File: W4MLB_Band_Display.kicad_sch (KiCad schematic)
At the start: 15 parts, among them J1 SSW-115-01-G-S, J2 SSW-115-01-G-S, J3 SSQ-108-01-T-D-LL, J4 SAMTEC-TST-108-01-X-D, J5 EJ503B, J6 796683-2, J7 PJRAN1X1U01X, J8 PJRAN1X1U01X, J9 Conn_01x10_Pin, U1 ESP32-DEVKIT-V1

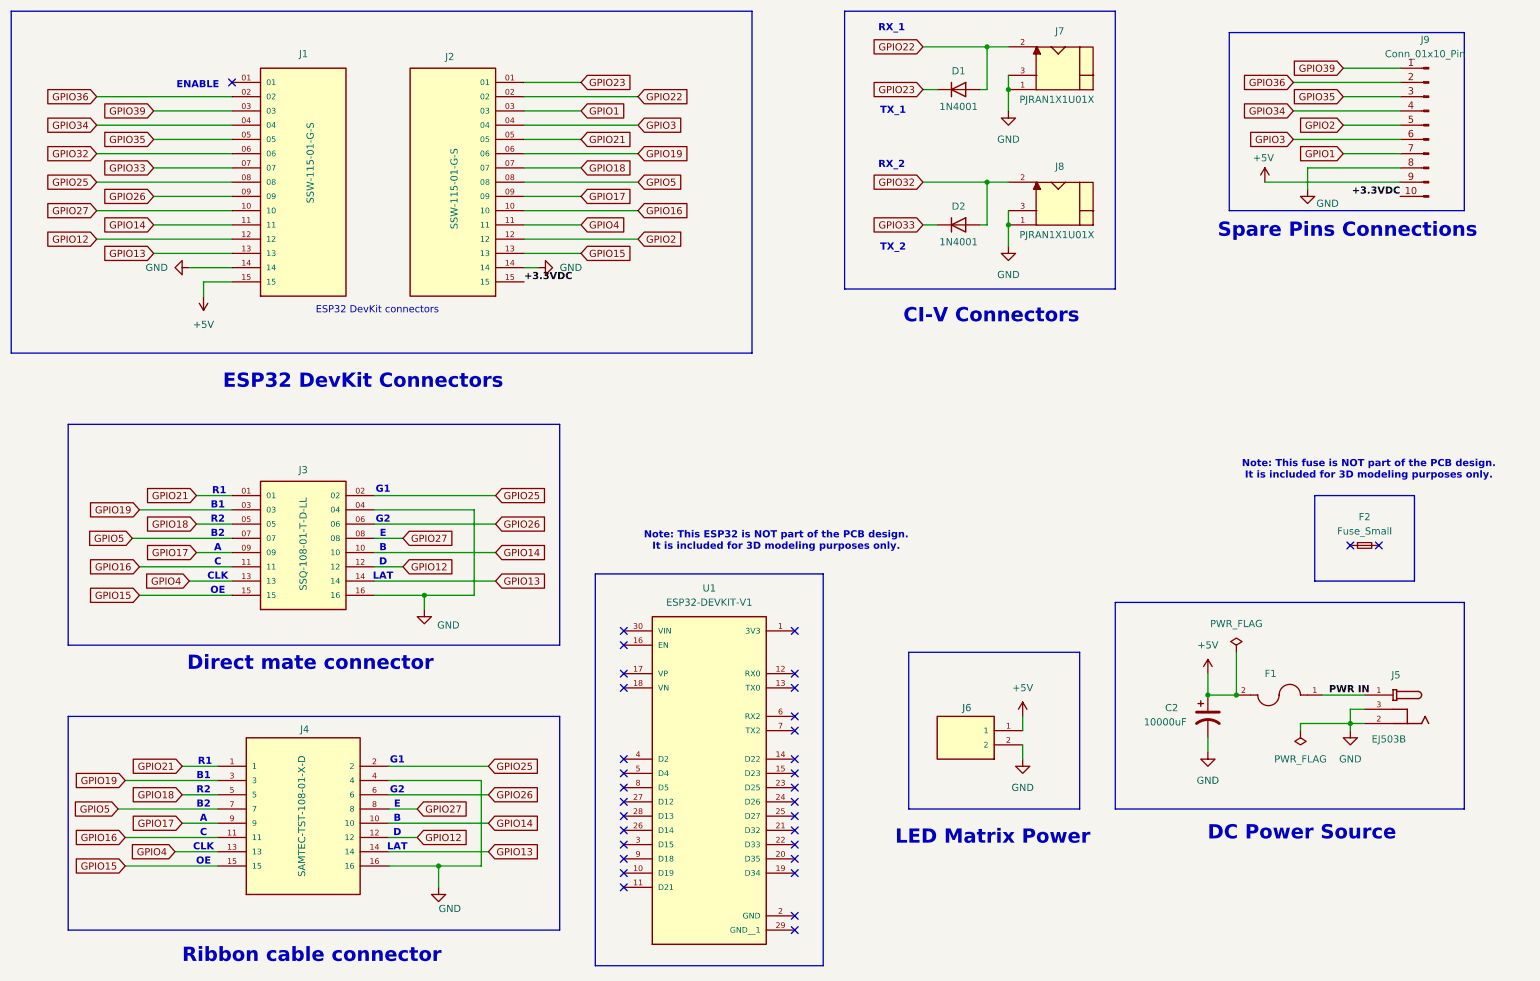
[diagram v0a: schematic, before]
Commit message: First release candidate draft
Laid out components and routed signals. Added silkscreen text and artwork
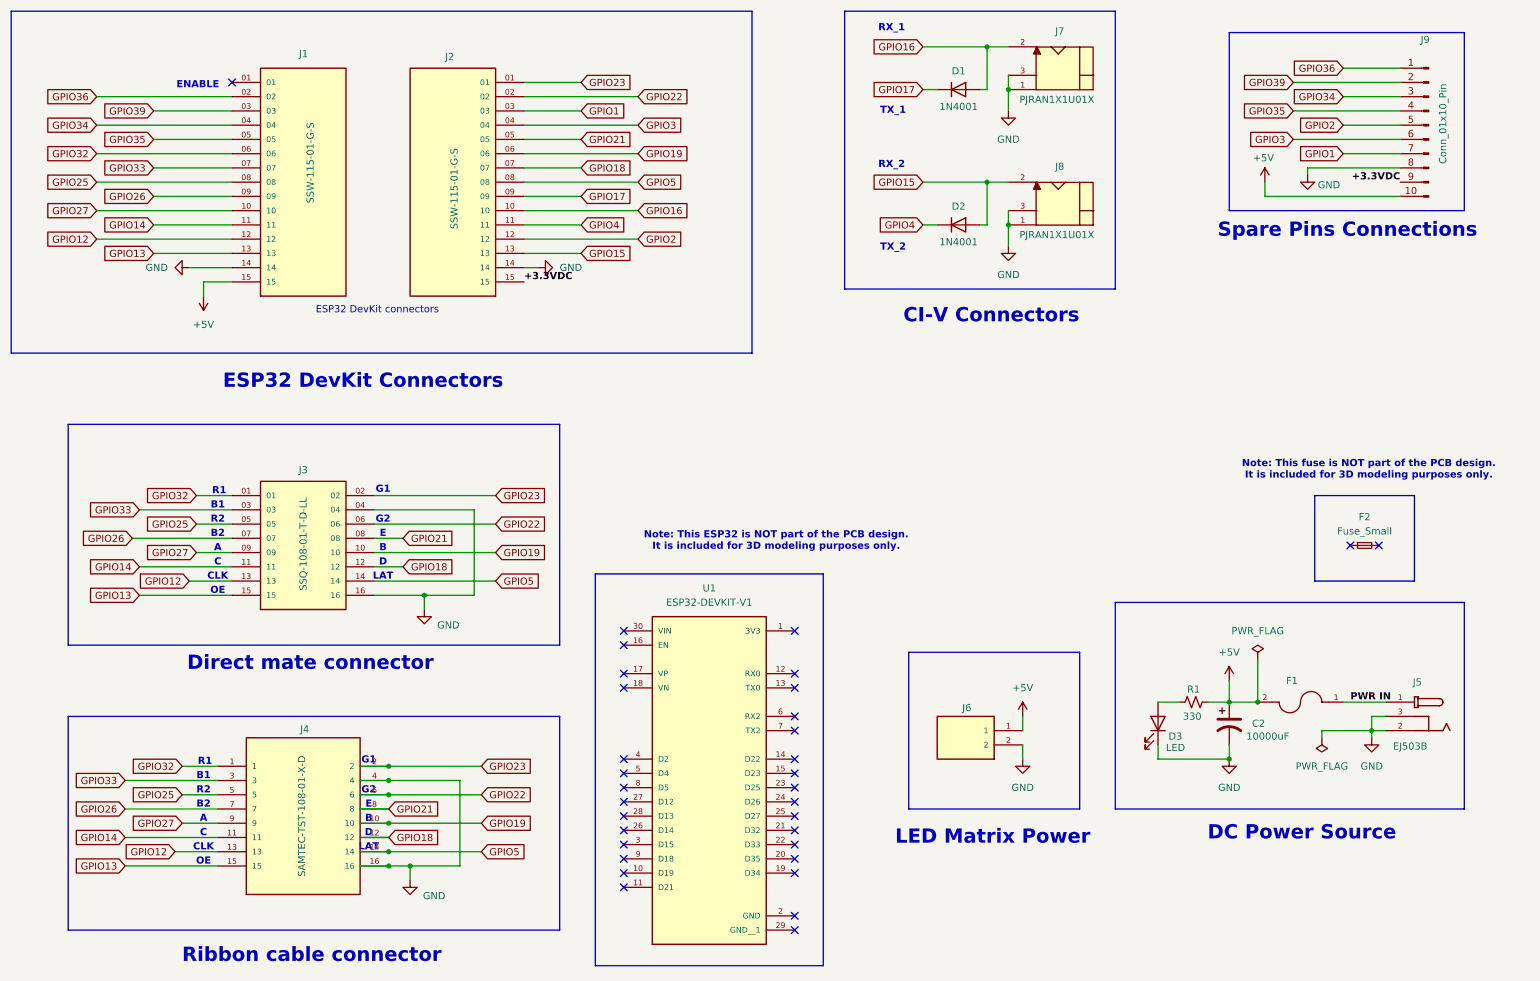
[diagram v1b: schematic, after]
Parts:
- added D3: LED, LED_SMD:LED_0805_2012Metric_Pad1.15x1.40mm_HandSolder, symbol Device:LED
- added R1: 330, Resistor_SMD:R_0805_2012Metric_Pad1.20x1.40mm_HandSolder, symbol Device:R_Small_US
- D1, D2: footprint Diode_THT:D_DO-41_SOD81_P10.16mm_Horizontal -> Diode_SMD:D_0805_2012Metric_Pad1.15x1.40mm_HandSolder
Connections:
- net +3.3VDC: now also J9.9 (Pin_9); no longer J9.10 (Pin_10)
- net +5V: now also J9.10 (Pin_10), R1.2; no longer J9.9 (Pin_9)
- net GND: now also D3.1 (K)
- net GPIO12: now also J3.13, J4.13; no longer J3.12, J4.12
- net GPIO13: now also J3.15, J4.15; no longer J3.14, J4.14
- net GPIO14: now also J3.11, J4.11; no longer J3.10, J4.10
- net GPIO15: now also D2.2 (A), J8.2; no longer J3.15, J4.15
- net GPIO16: now also D1.2 (A), J7.2; no longer J3.11, J4.11
- net GPIO17: now also D1.1 (K); no longer J3.09, J4.9
- net GPIO18: now also J3.12, J4.12; no longer J3.05, J4.5
- net GPIO19: now also J3.10, J4.10; no longer J3.03, J4.3
- net GPIO21: now also J3.08, J4.8; no longer J3.01, J4.1
- net GPIO22: now also J3.06, J4.6; no longer D1.2 (A), J7.2
- net GPIO23: now also J3.02, J4.2; no longer D1.1 (K)
- net GPIO25: now also J3.05, J4.5; no longer J3.02, J4.2
- net GPIO26: now also J3.07, J4.7; no longer J3.06, J4.6
- net GPIO27: now also J3.09, J4.9; no longer J3.08, J4.8
- net GPIO32: now also J3.01, J4.1; no longer D2.2 (A), J8.2
- net GPIO33: now also J3.03, J4.3; no longer D2.1 (K)
- net GPIO34: now also J9.3 (Pin_3); no longer J9.4 (Pin_4)
- net GPIO35: now also J9.4 (Pin_4); no longer J9.3 (Pin_3)
- net GPIO36: now also J9.1 (Pin_1); no longer J9.2 (Pin_2)
- net GPIO39: now also J9.2 (Pin_2); no longer J9.1 (Pin_1)
- net GPIO4: now also D2.1 (K); no longer J3.13, J4.13
- net GPIO5: now also J3.14, J4.14; no longer J3.07, J4.7
- new net: D3.2 (A), R1.1
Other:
- moved on the sheet: C2, F1, J5

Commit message: Buzzer
Added buzzer. Rearranged pins to make use of INPUT only pins for RX. Also reallocated different pins to the spare pins header and placed it in a better location.
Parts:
- added BZ1: Buzzer, Buzzer_Beeper:Buzzer_12x9.5RM7.6, symbol Device:Buzzer
- F2, U1: now not fitted; now left out of the parts list
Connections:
- net GND: now also J9.7 (Pin_7), BZ1.2 (-); no longer J9.8 (Pin_8)
- net GPIO1: now also J9.5 (Pin_5); no longer J9.7 (Pin_7)
- net GPIO15: now also J3.14, J4.14; no longer D2.2 (A), J8.2
- net GPIO16: now also J3.10, J4.10; no longer D1.2 (A), J7.2
- net GPIO17: now also J3.08, J4.8; no longer D1.1 (K)
- net GPIO18: now also J3.02, J4.2; no longer J3.12, J4.12
- net GPIO19: now also D2.1 (K), BZ1.1 (+); no longer J3.10, J4.10
- net GPIO2: now also J9.8 (Pin_8); no longer J9.5 (Pin_5)
- net GPIO21: now also J9.3 (Pin_3); no longer J3.08, J4.8
- net GPIO22: now also J9.4 (Pin_4); no longer J3.06, J4.6
- net GPIO23: now also D1.1 (K); no longer J3.02, J4.2
- net GPIO34: now also D1.2 (A), J7.2; no longer J9.3 (Pin_3)
- net GPIO35: now also D2.2 (A), J8.2; no longer J9.4 (Pin_4)
- net GPIO4: now also J3.12, J4.12; no longer D2.1 (K)
- net GPIO5: now also J3.06, J4.6; no longer J3.14, J4.14
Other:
- note added: "* INPUT ONLY PINS"
- note added: "*ENABLE"
- note added: "*RX_1"
- note added: "*RX_2"
- note added: "*VN"
- note added: "*VP"
- note added: "BUILTIN LED"
- note added: "Band Conflict Buzzer"
- note added: "Note: Diode blocks source current from TX pin. TX can only sink current. This is compatible with pull up on CI-V line."
- note added: "Note: GPIO36 & GPIO39 are INPUT only."
- note added: "RX"
- note added: "SCL"
- note added: "SDA"
- note added: "Spare Pins Connector"
- note added: "TX"
- note added: "Vin"
- note removed: "ENABLE"
- note removed: "Spare Pins Connections"
- company: (none) -> DL Designs

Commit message: Finisghing touches
Added fillets and chamfers to Cu zones. Adjusted silkscreen text and graphics.
Added mounting holes.
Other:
- title: PCARS Radio Station Band/Mode Display -> PCARS Radio Station Band/Mode Display Controller Board
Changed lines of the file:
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@@
 	(paper "A4")
 	(title_block
-		(title "PCARS Radio Station Band/Mode Display")
+		(title "PCARS Radio Station Band/Mode Display Controller Board")
 		(date "2025-04-17")
 		(rev "1.0")
